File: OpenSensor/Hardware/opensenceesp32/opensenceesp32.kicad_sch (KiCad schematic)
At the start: 20 parts, among them J1 Conn_01x08, Q1 AO3400A, Q2 AO3400A, SW1 SW_Push, SW2 SW_Push_Open, U1 L80-R, U2 LM1117DT-3.3, U3 LM1117DT-5.0, U4 ESP32_C3_OLED

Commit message: First draft of board
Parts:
- added J2: Conn_01x02, Connector_PinSocket_2.54mm:PinSocket_1x02_P2.54mm_Vertical, symbol Connector_Generic:Conn_01x02
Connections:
- net GND: now also J2.2 (Pin_2)
- net VCC: now also J2.1 (Pin_1)
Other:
- moved on the sheet: SW2

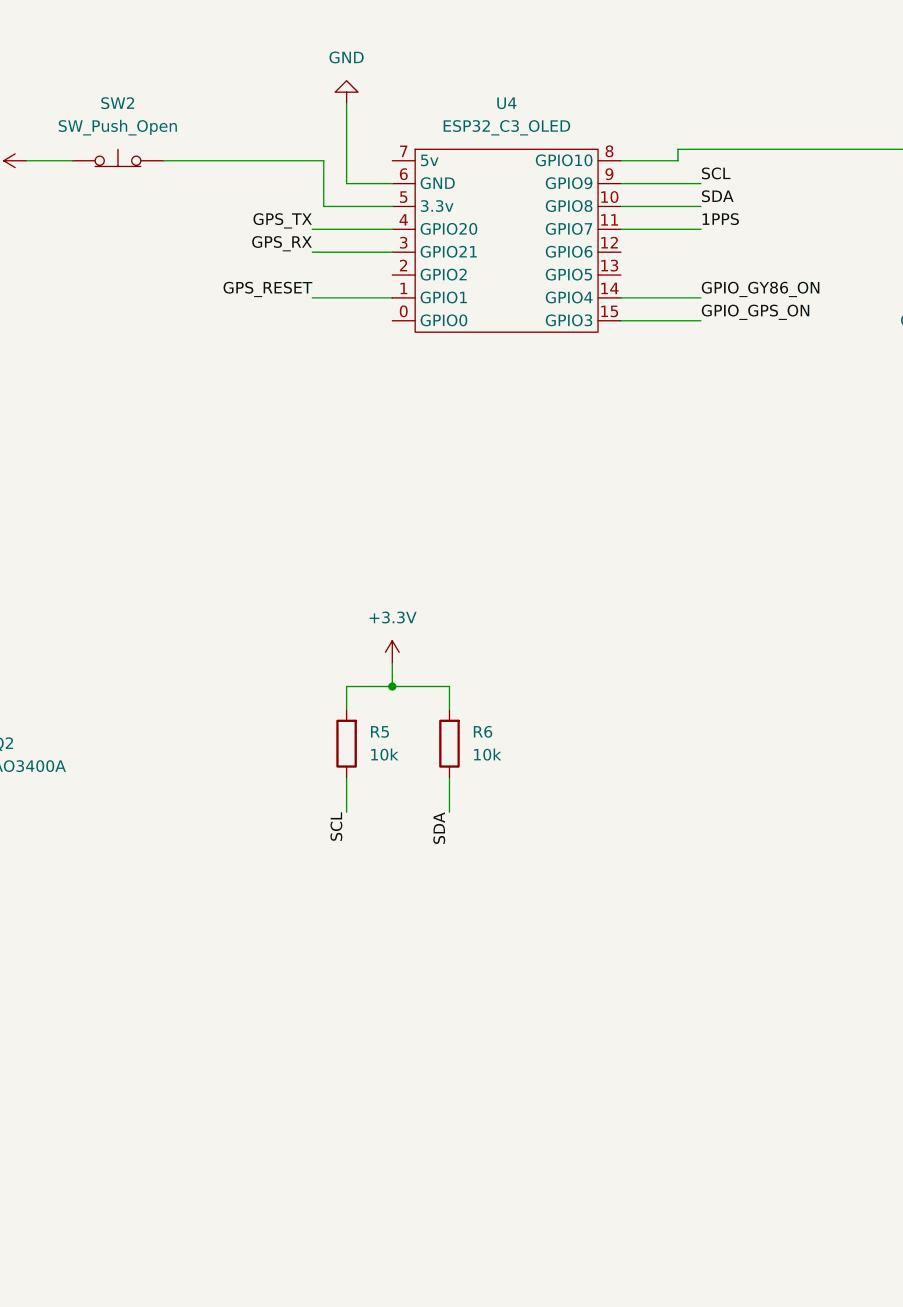
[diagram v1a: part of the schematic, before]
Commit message: moving to 0.2 for change in pins and adding daylight sensor
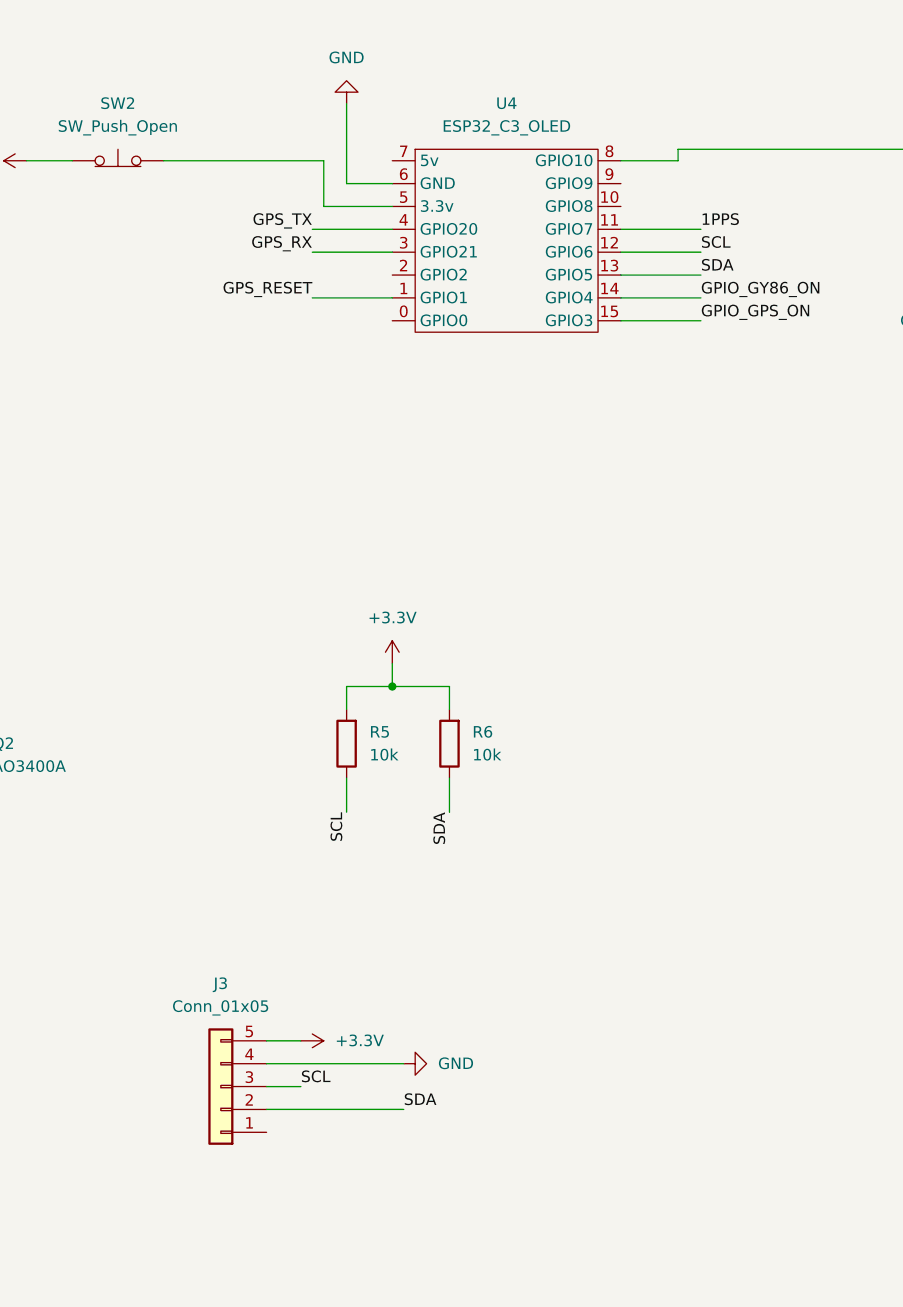
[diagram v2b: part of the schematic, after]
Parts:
- added J3: Conn_01x05, symbol Connector_Generic:Conn_01x05
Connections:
- net +3.3V: now also J3.5 (Pin_5)
- net GND: now also J3.4 (Pin_4)
- net SCL: now also U4.12 (GPIO6), J3.3 (Pin_3); no longer U4.9 (GPIO9)
- net SDA: now also U4.13 (GPIO5), J3.2 (Pin_2); no longer U4.10 (GPIO8)

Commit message: musings on esp32-c6
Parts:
- removed Q2: AO3400A, Package_TO_SOT_SMD:SOT-23, symbol Transistor_FET:AO3400A
- removed R2: 2.2k, Resistor_SMD:R_1206_3216Metric_Pad1.30x1.75mm_HandSolder, symbol Device:R
- removed R3: 100k, Resistor_SMD:R_1206_3216Metric_Pad1.30x1.75mm_HandSolder, symbol Device:R
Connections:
- net GPIO_GY86_ON: no longer names the net of U4.14 (GPIO4)
